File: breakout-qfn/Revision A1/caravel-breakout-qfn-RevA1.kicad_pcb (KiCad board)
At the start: 2 copper layers, 45 x 52.5 mm, 42 parts, among them CON1 REF-182665-01, CON2 REF-182665-01, CON3 73251-1352, U1 Caravel, U2 TLV73318PDBV

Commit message: WIP checkin for comments
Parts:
- U1: value Caravel -> Caravel_QFN; footprint ok-chips:Caravel_WLCSP -> Package_DFN_QFN:QFN-64-1EP_9x9mm_P0.5mm_EP7.65x7.65mm
- moved C3 41.0 mm to (59.0, -33.5)
- moved C1 39.0 mm to (58.0, -37.5)
- moved C2 36.7 mm to (58.0, -41.5)
- moved C5 36.4 mm to (58.5, -29.0)
- moved C7 36.1 mm to (58.0, -14.0), turned to -90 degrees
- moved C4 33.2 mm to (58.0, -24.5)
- moved C6 32.9 mm to (58.0, -19.0)
- moved C8 8.38 mm to (60.5, -5.00)
- moved U2 6.03 mm to (55.9, -6.54)
- moved C9 3.89 mm to (60.5, -7.51)
- moved U1 2.50 mm to (22.5, -30.5)
- moved CON3 0.50 mm to (22.5, -6.00)
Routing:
- net GND: track 7.66 -> 0.00 mm, vias 77 -> 73
- net mprj_io[15]: track 5.92 -> 0.00 mm
- net vdda2: track 4.47 -> 0.00 mm, vias 1 -> 0
- net vccd1: track 4.28 -> 0.00 mm, vias 1 -> 0
- net vdda1: track 3.79 -> 0.00 mm, vias 1 -> 0
- net Caravel_SCK: track 3.75 -> 0.00 mm
- net mprj_io[36]: track 3.09 -> 0.00 mm
- net mprj_io[34]: track 3.04 -> 0.00 mm
- net mprj_io[14]: track 2.96 -> 0.00 mm
- net Caravel_D1: track 2.87 -> 0.00 mm
- net mprj_io[13]: track 2.80 -> 0.00 mm
- net mprj_io[0]: track 2.80 -> 0.00 mm
- net mprj_io[33]: track 2.64 -> 0.00 mm
- net mprj_io[35]: track 2.59 -> 0.00 mm
- net vccd: track 2.59 -> 0.00 mm, vias 1 -> 0
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
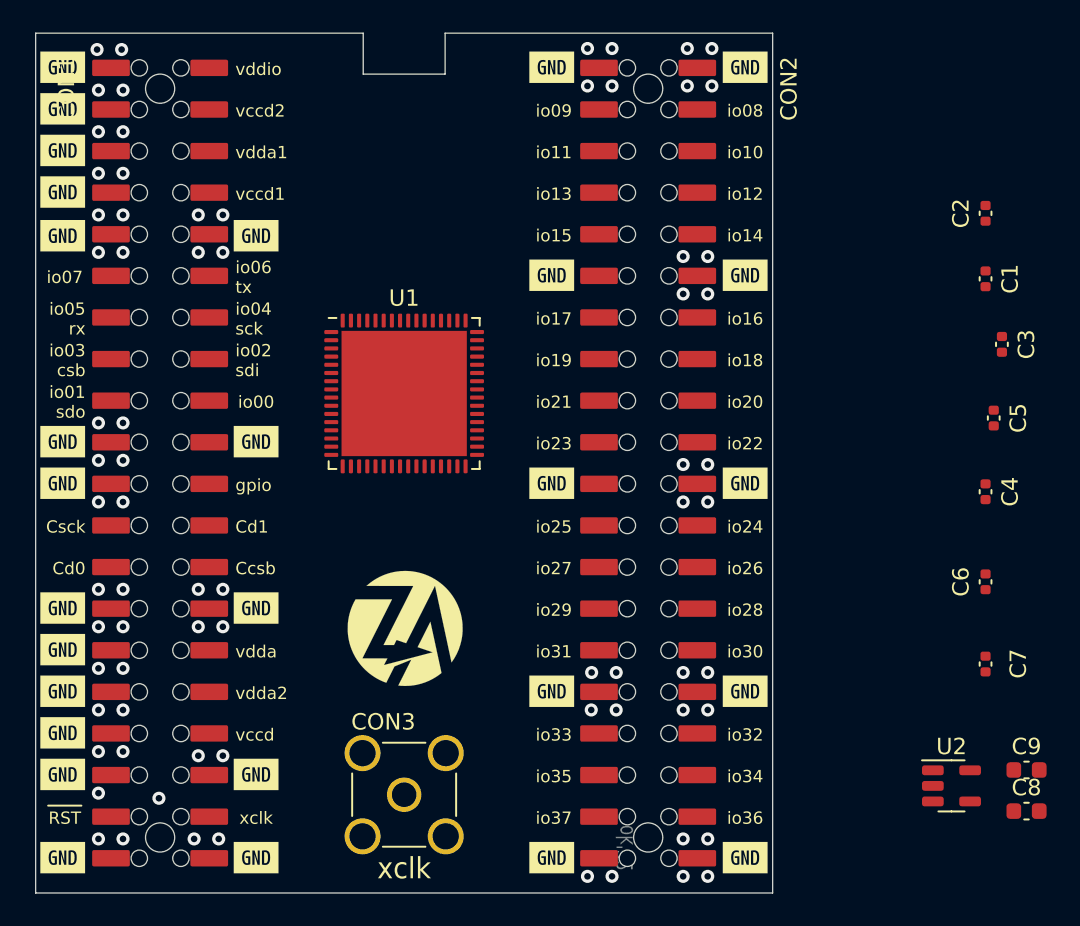
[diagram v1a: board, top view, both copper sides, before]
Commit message: kicad 7 migration, qfn symbol and wiring
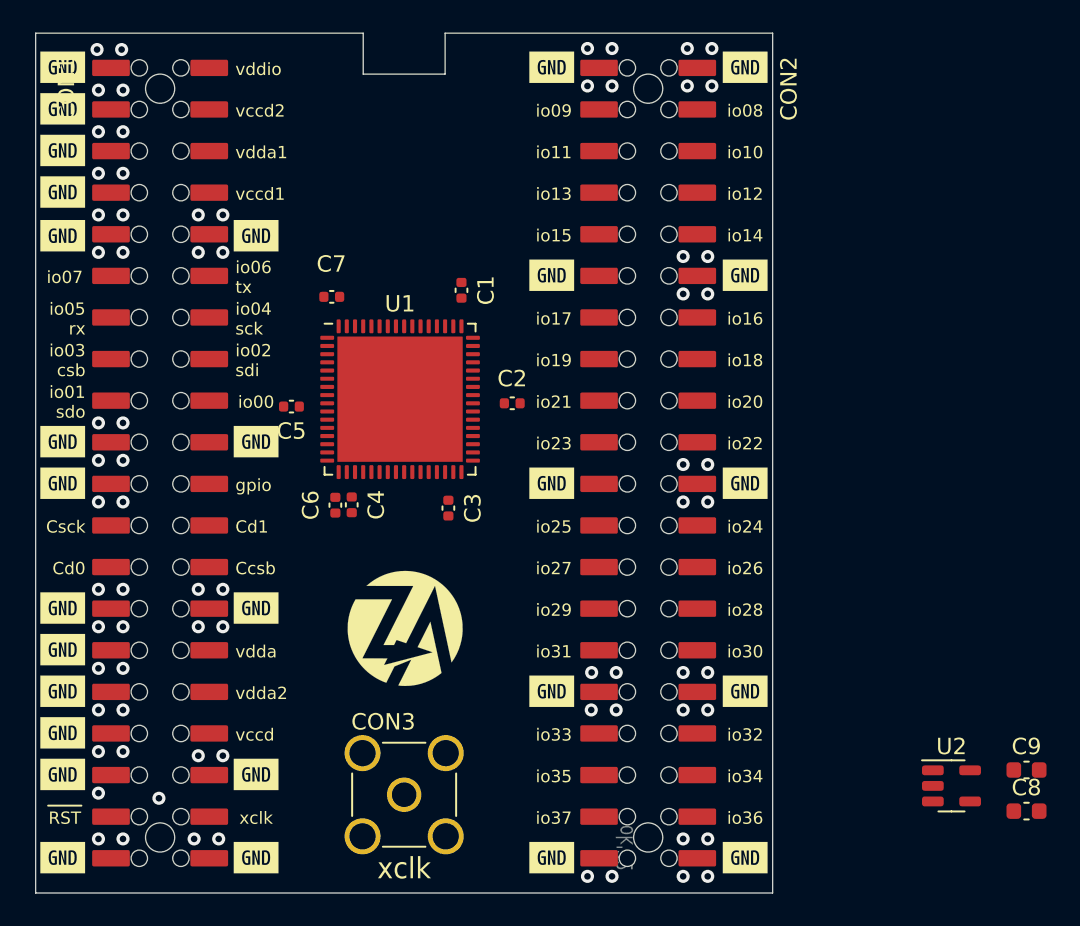
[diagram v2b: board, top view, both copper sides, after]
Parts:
- moved C7 45.8 mm to (18.1, -36.4), turned to 0 degrees
- moved C5 42.9 mm to (15.6, -29.7), turned to 0 degrees
- moved C6 40.0 mm to (18.3, -23.7)
- moved C4 38.7 mm to (19.3, -23.7)
- moved C3 35.2 mm to (25.2, -23.5)
- moved C1 32.0 mm to (26.0, -36.8)
- moved C2 31.1 mm to (29.1, -29.9), turned to 0 degrees
- moved U1 0.43 mm to (22.2, -30.1)
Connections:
- U1 pad 1: unconnected-(U1-Pad1) -> GND
- U1 pad 10: unconnected-(U1-Pad10) -> GND
- U1 pad 11: unconnected-(U1-Pad11) -> mprj_io[32]
- U1 pad 12: unconnected-(U1-Pad12) -> mprj_io[33]
- U1 pad 13: unconnected-(U1-Pad13) -> mprj_io[34]
- U1 pad 14: unconnected-(U1-Pad14) -> mprj_io[35]
- U1 pad 15: unconnected-(U1-Pad15) -> mprj_io[36]
- U1 pad 16: unconnected-(U1-Pad16) -> mprj_io[37]
- U1 pad 17: unconnected-(U1-Pad17) -> vddio
- U1 pad 18: unconnected-(U1-Pad18) -> vccd
- U1 pad 2: unconnected-(U1-Pad2) -> mprj_io[25]
- U1 pad 20: unconnected-(U1-Pad20) -> GND
- U1 pad 21: unconnected-(U1-Pad21) -> ~{RST}
- U1 pad 22: unconnected-(U1-Pad22) -> xclk
- U1 pad 23: unconnected-(U1-Pad23) -> GND
- U1 pad 24: unconnected-(U1-Pad24) -> Caravel_CSB
- U1 pad 25: unconnected-(U1-Pad25) -> Caravel_SCK
- U1 pad 26: unconnected-(U1-Pad26) -> Caravel_D0
- U1 pad 27: unconnected-(U1-Pad27) -> Caravel_D1
- U1 pad 28: unconnected-(U1-Pad28) -> gpio
- U1 pad 29: unconnected-(U1-Pad29) -> GND
- U1 pad 3: unconnected-(U1-Pad3) -> mprj_io[26]
- U1 pad 30: unconnected-(U1-Pad30) -> vdda
- U1 pad 31: unconnected-(U1-Pad31) -> mprj_io[0]
- U1 pad 32: unconnected-(U1-Pad32) -> mprj_io[1]_SDO
- U1 pad 33: unconnected-(U1-Pad33) -> mprj_io[2]_SDI
- U1 pad 34: unconnected-(U1-Pad34) -> mprj_io[3]_CSB
- U1 pad 35: unconnected-(U1-Pad35) -> mprj_io[4]_SCK
- U1 pad 36: unconnected-(U1-Pad36) -> mprj_io[5]_ser_rx
- U1 pad 37: unconnected-(U1-Pad37) -> mprj_io[6]_ser_tx
- U1 pad 38: unconnected-(U1-Pad38) -> GND
- U1 pad 39: unconnected-(U1-Pad39) -> GND
- U1 pad 4: unconnected-(U1-Pad4) -> mprj_io[27]
- U1 pad 40: unconnected-(U1-Pad40) -> vdda1
- U1 pad 41: unconnected-(U1-Pad41) -> mprj_io[7]
- U1 pad 42: unconnected-(U1-Pad42) -> mprj_io[8]
- U1 pad 43: unconnected-(U1-Pad43) -> mprj_io[9]
- U1 pad 44: unconnected-(U1-Pad44) -> mprj_io[10]
- U1 pad 45: unconnected-(U1-Pad45) -> mprj_io[11]
- U1 pad 46: unconnected-(U1-Pad46) -> mprj_io[12]
- U1 pad 48: unconnected-(U1-Pad48) -> mprj_io[13]
- U1 pad 49: unconnected-(U1-Pad49) -> vccd1
- U1 pad 5: unconnected-(U1-Pad5) -> mprj_io[28]
- U1 pad 50: unconnected-(U1-Pad50) -> mprj_io[14]
- U1 pad 51: unconnected-(U1-Pad51) -> mprj_io[15]
- U1 pad 53: unconnected-(U1-Pad53) -> mprj_io[16]
- U1 pad 54: unconnected-(U1-Pad54) -> mprj_io[17]
- U1 pad 55: unconnected-(U1-Pad55) -> mprj_io[18]
- U1 pad 56: unconnected-(U1-Pad56) -> GND
- U1 pad 57: unconnected-(U1-Pad57) -> mprj_io[19]
- U1 pad 58: unconnected-(U1-Pad58) -> mprj_io[20]
- U1 pad 59: unconnected-(U1-Pad59) -> mprj_io[21]
- U1 pad 6: unconnected-(U1-Pad6) -> mprj_io[29]
- U1 pad 60: unconnected-(U1-Pad60) -> mprj_io[22]
- U1 pad 61: unconnected-(U1-Pad61) -> mprj_io[23]
- U1 pad 62: unconnected-(U1-Pad62) -> mprj_io[24]
- U1 pad 63: unconnected-(U1-Pad63) -> vccd2
- U1 pad 7: unconnected-(U1-Pad7) -> mprj_io[30]
- U1 pad 8: unconnected-(U1-Pad8) -> mprj_io[31]
- U1 pad 9: unconnected-(U1-Pad9) -> vdda2
